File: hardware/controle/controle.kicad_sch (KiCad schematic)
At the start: 44 parts, among them J3 PWR, J4 DATA, J5 UART7, J6 TWI3, J7 SENS0375, J8 TWI4, J9 LED, U2 MCP7940N-xSN, U4 ULN2003, Y1 32.768Khz

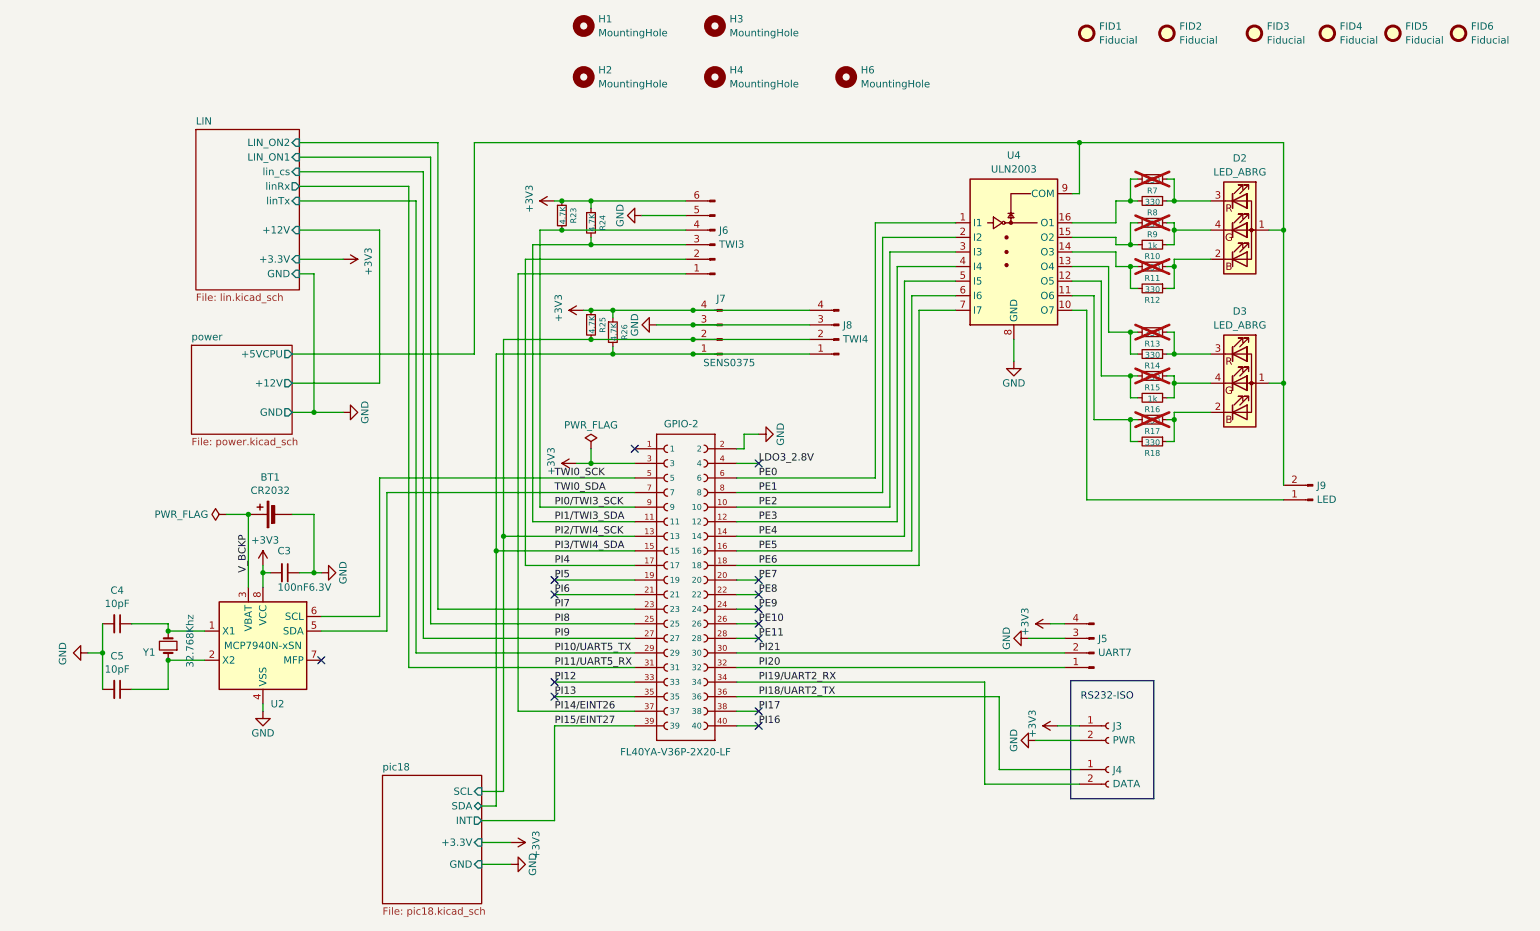
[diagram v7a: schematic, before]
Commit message: hardware/controle: control CPU power from pic18: - add a separate 3.3V power for pic18 - use the pic18 to start the tps54228
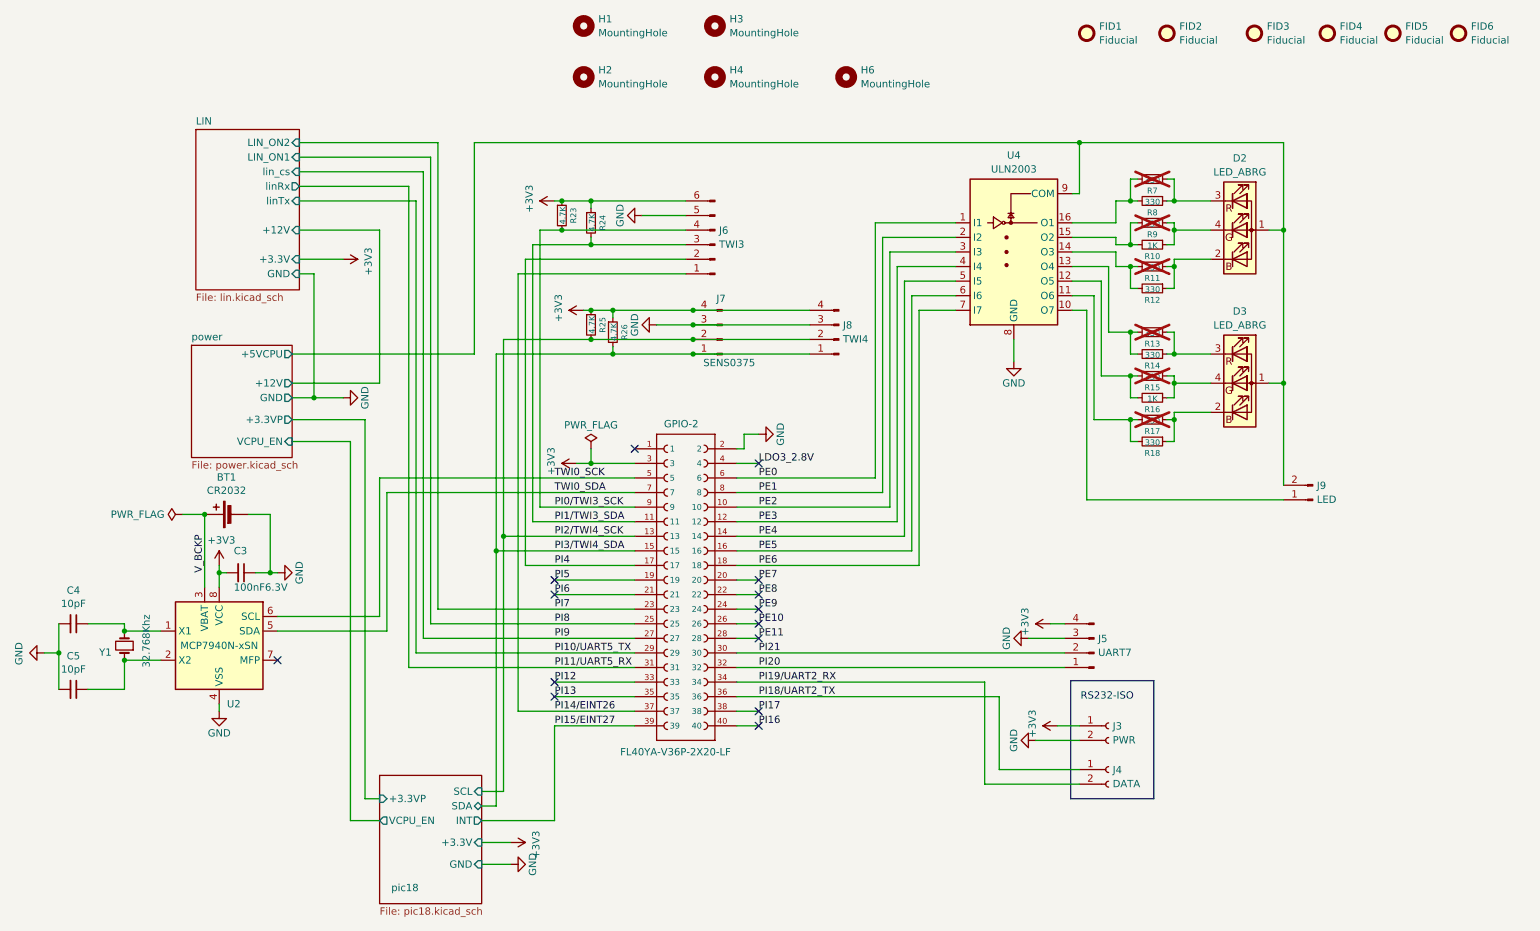
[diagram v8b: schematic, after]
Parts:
- R10, R16: value 1k -> 1K
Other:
- sheet pic18 ports: added +3.3VP, VCPU_EN; removed none
- sheet power ports: added +3.3VP, VCPU_EN; removed none
- moved on the sheet: BT1, C3, C4, C5, U2, Y1
